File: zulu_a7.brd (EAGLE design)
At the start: 61 x 25.4 mm, 183 parts, among them J1 Pmod 2x6, Q1 12MHz 25ppm (FPGA + FT2232HQ), Q2 2N7002, Q3 MBT3904DW1T1, U1 XC7A35T-1CPG236C, U10 93LC46BT-I/SN, U2 FT2232HQ USB-UART/JTAG Bridge, U3 AS4C32M16SB-6TIN, U4 W25Q128JVSIQ, U8 LTC3569EUDC#TRPBF, X1 Molex 105017-0001 Micro-USB-B

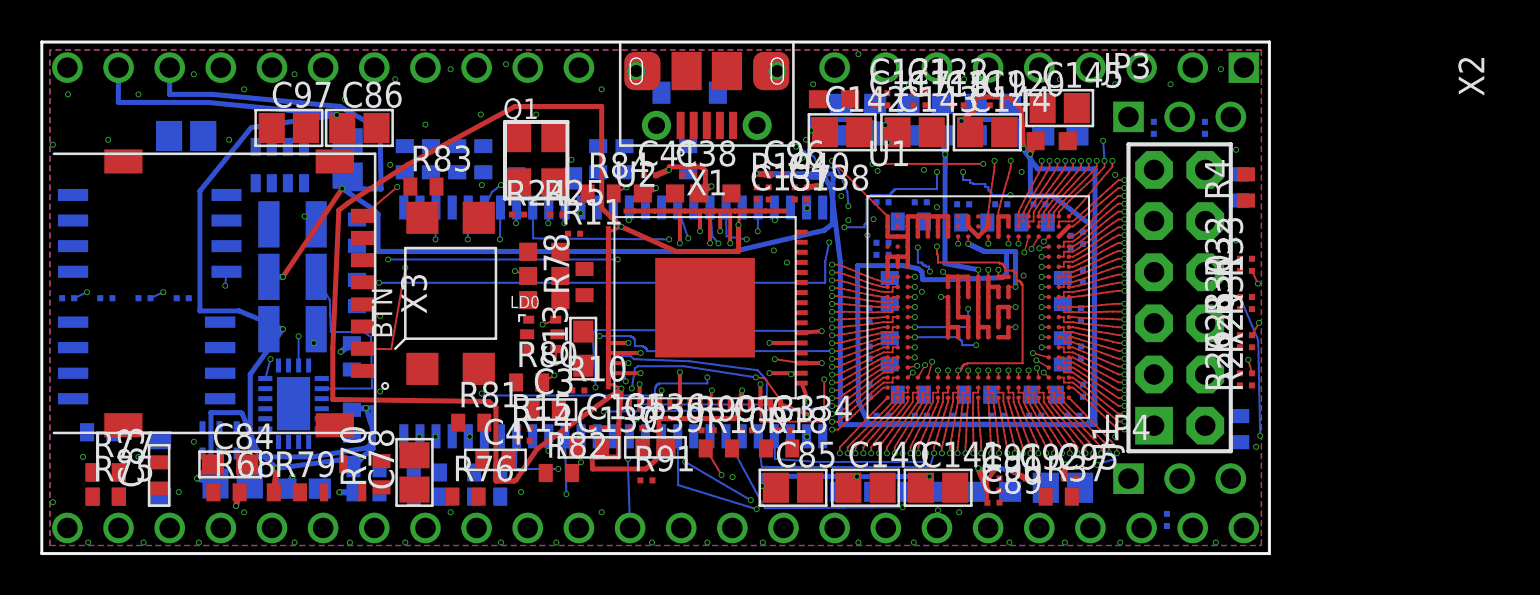
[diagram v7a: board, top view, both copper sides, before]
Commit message: signals.py: PathFinder gets the same final validation, from one shared helper
The greedy branch got a pass over the finished plan last commit; PathFinder
had the same exposure and a weaker guard than it looked. Its revert loop
compares WIRE AGAINST WIRE ON ONE LAYER -- vias never enter the comparison
-- and its remedy is to restore a net's unstraightened path, which silently
does nothing once neither net still has a raw path to go back to:
bad.add(...) runs, `if n in raw` fails, and three rounds pass without
changing anything or saying so. It also runs BEFORE pairplan is merged, so
the differential pair was never checked against the group at all. That gap
is where D10 vs SDRAM-CLK at -0.1000 came from.

validate_plan() is now defined once and called from both branches, so the
two routers cannot drift apart on this again. The revert loop stays where it
is -- putting straightening back is a better outcome than ripping a net up
when it works -- and validation runs after it to catch what survives.

It fires on four groups: sdram (A8, A2), x2 (CHAN25), microsd (SD-CMD) and
rest (LD5_TO_Q2, EE-CLK, EE-CS, PMOD-7).

AND THE BOARD COMES OUT BETTER ROUTED, which was not the point but is worth
recording: 24 of 175 signals bare against 27, because ripping two nets out
of the SDRAM bus early frees room that x2, microsd, jtag and rest all take
up (15->16, 3->4, 5->6, 11->14). check_board: 2546 wires, 390 vias, 0
findings.

Note that collides() is stricter than check_board -- 0.34 mm wire-to-via
against the 0.29 a 0.10 trace owes, because route[1] carries no per-segment
width -- so some of what it rips would have passed. That is the right way
round for a guard, and here it paid for itself anyway.

Co-Authored-By: Claude Opus 5 <noreply@anthropic.com>
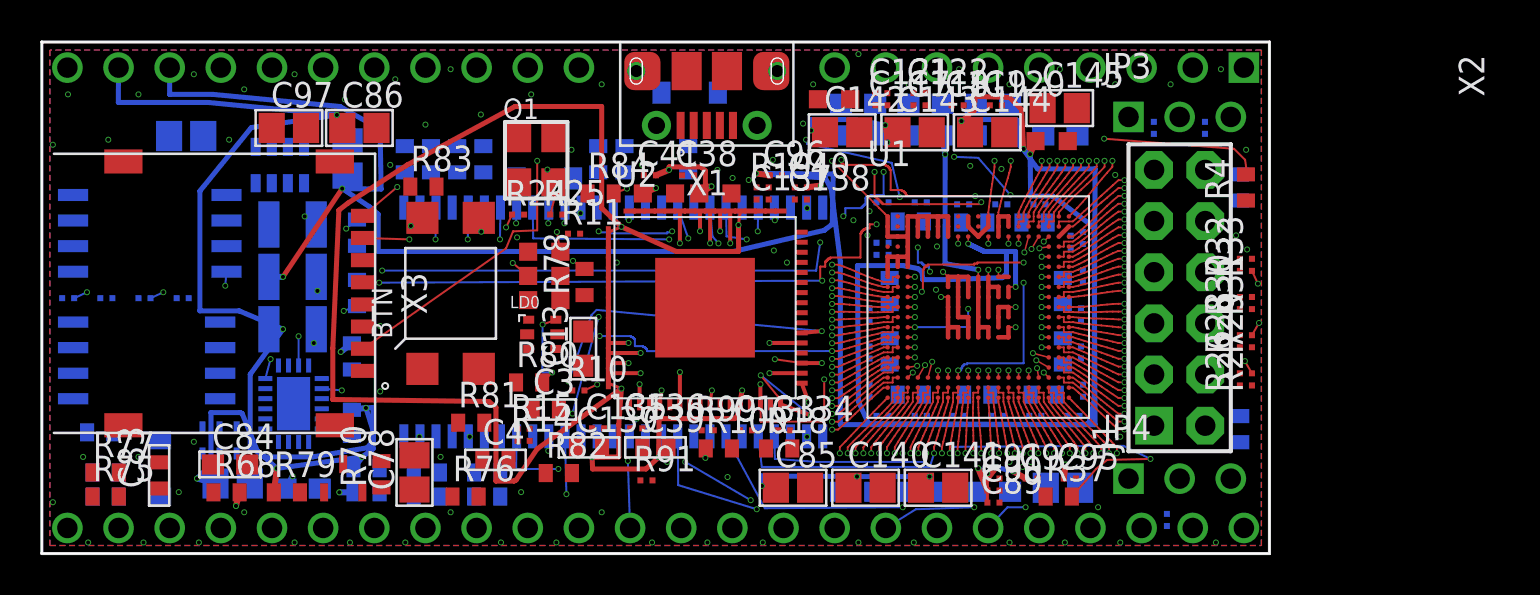
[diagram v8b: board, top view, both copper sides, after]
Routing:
- net FPGA-TMS: track 2.76 -> 63.2 mm, vias 1 -> 7
- net CHAN24: track 0.35 -> 49.5 mm, vias 1 -> 6
- net JA3: track 0.35 -> 49.3 mm, vias 1 -> 4
- net CHAN9: track 41.8 -> 0.35 mm, vias 4 -> 1
- net SD-DAT0: track 0.81 -> 39.8 mm, vias 1 -> 5
- net A8: track 33.9 -> 0.35 mm, vias 4 -> 1
- net CHAN6: track 31.9 -> 0.35 mm
- net SW2_NET: track 10.1 -> 37.3 mm, vias 0 -> 2
- net CHAN5: track 0.47 -> 27.5 mm, vias 1 -> 3
- net CHAN20: track 88.0 -> 61.3 mm, vias 8 -> 5
- net SW3_NET: track 35.4 -> 9.25 mm
- net ANALOG-IO0: track 0.00 -> 24.3 mm, vias 0 -> 1
- net JA4: track 0.35 -> 23.8 mm
- net JA7: track 22.6 -> 0.71 mm, vias 2 -> 1
- net A2: track 24.3 -> 4.06 mm, vias 3 -> 1
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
